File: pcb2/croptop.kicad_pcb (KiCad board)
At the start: 4 copper layers, 115.6 x 45.7 mm, 241 parts, among them J1 PICKit Header, J2 USB_A, J3 5V USB, J4 4-1734839-0, J5 Terminal Block, J6 DNP, J7 DNP, SW1 BTNA, SW2 BTNA, U1 PIC32MX795F512L, U10 AD7799, U11 74HCT125D, U12 Si7006-A20, U13 UCAM-M8Q, U14 W25N01GV, U15 LIS3DH, U16 PUSBM5V5X4, U17 DT6250-06MR-13, U18 PUSBM5V5X4, U2 REG71055, U3 FAN5333BSX, U4 MIC23050, U5 TC1014, U6 FT812Q, U8 74HCT125D, U9 DRV8872, Y1 CXO, Y2 12MHz

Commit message: Footprints done, board started
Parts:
- moved G*** 231.4 mm to (314.9, 130.8)
- moved G*** 201.3 mm to (333.2, 137.6)
- moved G*** 190.2 mm to (320.4, 156.0)
- moved G*** 169.3 mm to (314.4, 124.1)
- moved G*** 155.3 mm to (314.7, 139.0)
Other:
- board text added: "CROPTOP v2.0"

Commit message: Board almost done
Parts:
- removed C4: 26pF, Capacitor_SMD:C_0402_1005Metric
- removed D25: LED1, LED_SMD:LED_0805_2012Metric
- removed the G*** at (314.7, 139.0)
- removed the G*** at (314.4, 124.1)
- removed the G*** at (314.9, 130.8)
- removed TP100, TP73, TP74, TP78, TP82, TP83, TP85, TP86, TP88, TP89, TP90, TP91, TP92, TP99: TestPoint_Alt, croptop:TestPoint
- added C29: 0.1u, Capacitor_SMD:C_0402_1005Metric, F.Cu at (200.0, 109.0)
- added C31: 10u, Capacitor_SMD:C_1206_3216Metric, F.Cu at (201.3, 135.9)
- added C41: 0.1u, Capacitor_SMD:C_0402_1005Metric, F.Cu at (158.6, 83.1)
- added C42: 0.1u, Capacitor_SMD:C_0402_1005Metric, F.Cu at (162.1, 79.5)
- added C48: 10u, Capacitor_SMD:C_1206_3216Metric, F.Cu at (125.7, 137.8)
- added C55: 0.1u, Capacitor_SMD:C_0402_1005Metric, F.Cu at (174.0, 144.1)
- added C62: 10u, Capacitor_SMD:C_1206_3216Metric, F.Cu at (164.5, 145.4)
- added C64: 0.1u, Capacitor_SMD:C_0402_1005Metric, F.Cu at (207.0, 146.7)
- added C66: 10u, Capacitor_SMD:C_1206_3216Metric, F.Cu at (221.6, 148.6)
- added C67: 0.01u, Capacitor_SMD:C_0402_1005Metric, F.Cu at (79.4, 146.7)
- added C70: 0.1u, Capacitor_SMD:C_0805_2012Metric, F.Cu at (101.6, 137.8)
- added C72: 10u, Capacitor_SMD:C_1206_3216Metric, F.Cu at (215.9, 148.0)
- added C73: 100u, Capacitor_SMD:CP_Elec_6.3x7.7, F.Cu at (95.2, 138.4)
- added C74: 0.1u, Capacitor_SMD:C_0402_1005Metric, F.Cu at (90.8, 145.4)
- added C75: 0.1u, Capacitor_SMD:C_0402_1005Metric, F.Cu at (218.4, 151.1)
- added C76: 0.1u, Capacitor_SMD:C_0402_1005Metric, F.Cu at (90.8, 144.1)
- added C77: 0.1u, Capacitor_SMD:C_0402_1005Metric, F.Cu at (90.8, 142.9)
- added C78: 10u, Capacitor_SMD:C_1206_3216Metric, F.Cu at (77.5, 85.1)
- added C79: 10u, Capacitor_SMD:C_1206_3216Metric, F.Cu at (78.7, 79.4)
- added C80: 10u, Capacitor_SMD:C_1206_3216Metric, F.Cu at (77.5, 92.7)
- added C81: 0.1u, Capacitor_SMD:C_0402_1005Metric, F.Cu at (74.9, 87.6)
- added C82: 10u, Capacitor_SMD:C_1206_3216Metric, F.Cu at (83.8, 76.8)
- added C83: 10u, Capacitor_SMD:C_1206_3216Metric, F.Cu at (83.8, 62.9)
- added C84: 10u, Capacitor_SMD:C_1206_3216Metric, F.Cu at (78.7, 61.6)
- added C85: 10u, Capacitor_SMD:C_1206_3216Metric, F.Cu at (125.7, 64.8)
- added C86: 0.1u, Capacitor_SMD:C_0402_1005Metric, F.Cu at (125.7, 66.7)
- added C87: 0.1u, Capacitor_SMD:C_0402_1005Metric, F.Cu at (148.6, 63.5)
- added C88: 0.1u, Capacitor_SMD:C_0402_1005Metric, F.Cu at (117.9, 66.6)
- added C89: 10u, Capacitor_SMD:C_1206_3216Metric, F.Cu at (117.9, 64.8)
- added D10: TPD2E007, Package_TO_SOT_SMD:SOT-323_SC-70, F.Cu at (185.2, 89.9)
- added D11: TPD1E6B06, Diode_SMD:D_0201_0603Metric, F.Cu at (184.7, 92.7)
- added D12: TPD1E6B06, Diode_SMD:D_0201_0603Metric, F.Cu at (143.5, 148.6)
- added D13: TPD1E6B06, Diode_SMD:D_0201_0603Metric, F.Cu at (125.7, 148.6)
- added D14: TPD1E6B06, Diode_SMD:D_0201_0603Metric, F.Cu at (164.5, 148.6)
- added D15: NSR0240HT1G, Diode_SMD:D_SMA, F.Cu at (98.4, 143.8)
- added D16: TPD1E6B06, Diode_SMD:D_0201_0603Metric, F.Cu at (218.4, 152.4)
- added D17: TPD2E007, Package_TO_SOT_SMD:SOT-323_SC-70, F.Cu at (109.2, 149.2)
- added D18: TPD2E007, Package_TO_SOT_SMD:SOT-323_SC-70, F.Cu at (96.5, 149.2)
- added D19: TPD2E007, Package_TO_SOT_SMD:SOT-323_SC-70, F.Cu at (91.4, 149.2)
- added D20: TPD2E007, Package_TO_SOT_SMD:SOT-323_SC-70, F.Cu at (78.7, 149.2)
- added D21: TPD1E6B06, Diode_SMD:D_0201_0603Metric, F.Cu at (73.7, 87.3)
- added D22: LTSTC190KGKT, LED_SMD:LED_0603_1608Metric, F.Cu at (73.3, 102.5)
- added D23: LTSTC190KGKT, LED_SMD:LED_0603_1608Metric, F.Cu at (80.9, 102.5)
- added D3: TPD1E6B06, Diode_SMD:D_0201_0603Metric, F.Cu at (236.9, 94.3)
- added D4: LTSTC190KGKT, LED_SMD:LED_0603_1608Metric, F.Cu at (200.7, 123.1)
- added D5: NSR0240HT1G, Diode_SMD:D_SMA, F.Cu at (195.6, 105.4)
- added D6: TPD1E6B06, Diode_SMD:D_0201_0603Metric, F.Cu at (228.7, 126.8)
- added D8: LTSTC190KGKT, LED_SMD:LED_0603_1608Metric, F.Cu at (200.7, 126.2)
- added F1: MF-NSMF110, croptop:Bourns_Fuse, F.Cu at (233.7, 96.5)
- added J10: 1702474, croptop:solderless_terminal, F.Cu at (209.6, 158.1)
- added J11: 1702474, croptop:solderless_terminal, F.Cu at (191.8, 158.1)
- added J12: 1702474, croptop:solderless_terminal, F.Cu at (174.0, 158.1)
- added J13: 1702474, croptop:solderless_terminal, F.Cu at (102.9, 158.1)
- added J14: 1702474, croptop:solderless_terminal, F.Cu at (85.1, 158.1)
- added J15: TSM-112-01-L-DV, Connector_PinHeader_2.54mm:PinHeader_2x12_P2.54mm_Vertical_SMD, F.Cu at (97.2, 69.8)
- added J16: DM3D-SF, Connector_Card:microSD_HC_Hirose_DM3D-SF, F.Cu at (62.2, 92.1)
- added J8: 1702474, croptop:solderless_terminal, F.Cu at (138.4, 158.1)
- added J9: 1702474, croptop:solderless_terminal, F.Cu at (120.7, 158.1)
- added JP1: Solder Jumper, Jumper:SolderJumper-3_P1.3mm_Bridged12_RoundedPad1.0x1.5mm, F.Cu at (169.5, 135.9)
- added L10: BKP1005HS121, Inductor_SMD:L_0402_1005Metric, F.Cu at (150.5, 64.8)
- added L4: BKP1005HS121, Inductor_SMD:L_0402_1005Metric, F.Cu at (197.6, 133.3)
- added L5: BLM15HD102SN1D, Inductor_SMD:L_0402_1005Metric, F.Cu at (145.8, 69.3)
- added L6: BLM15HD102SN1D, Inductor_SMD:L_0402_1005Metric, F.Cu at (145.8, 66.3)
- added L7: BLM15HD102SN1D, Inductor_SMD:L_0402_1005Metric, F.Cu at (145.8, 65.3)
- added L8: BLM15HD102SN1D, Inductor_SMD:L_0402_1005Metric, F.Cu at (131.3, 68.3)
- added L9: BLM15HD102SN1D, Inductor_SMD:L_0402_1005Metric, F.Cu at (138.4, 74.7)
- added Q1: BSS138, Package_TO_SOT_SMD:SOT-23, F.Cu at (102.9, 132.1)
- added Q2: BSS84, Package_TO_SOT_SMD:SOT-23, F.Cu at (108.0, 132.1)
- added Q3: Q2319ADS-T1-GE3, Package_TO_SOT_SMD:SOT-23, F.Cu at (100.3, 148.0)
- added Q4: BSS138, Package_TO_SOT_SMD:SOT-23, F.Cu at (72.0, 106.4)
- added Q5: BSS138, Package_TO_SOT_SMD:SOT-23, F.Cu at (80.2, 106.4)
- added Q6: BSS138, Package_TO_SOT_SMD:SOT-23, F.Cu at (87.5, 106.4)
- added R100: 220, Resistor_SMD:R_0402_1005Metric, F.Cu at (111.1, 76.8)
- added R101: 220, Resistor_SMD:R_0402_1005Metric, F.Cu at (111.1, 62.9)
- added R102: 22, Resistor_SMD:R_0402_1005Metric, F.Cu at (69.8, 95.9)
- added R103: 22, Resistor_SMD:R_0402_1005Metric, F.Cu at (69.8, 90.8)
- added R104: 220, Resistor_SMD:R_0402_1005Metric, F.Cu at (108.6, 62.9)
- added R105: 22, Resistor_SMD:R_0402_1005Metric, F.Cu at (69.8, 93.3)
- added R106: 22, Resistor_SMD:R_0402_1005Metric, F.Cu at (69.8, 88.3)
- added R107: 220, Resistor_SMD:R_0402_1005Metric, F.Cu at (90.8, 63.0)
- added R108: 220, Resistor_SMD:R_0402_1005Metric, F.Cu at (95.9, 63.0)
- added R109: 220, Resistor_SMD:R_0402_1005Metric, F.Cu at (101.0, 62.9)
- added R110: 220, Resistor_SMD:R_0402_1005Metric, F.Cu at (106.0, 62.9)
- added R111: 220, Resistor_SMD:R_0402_1005Metric, F.Cu at (88.3, 63.0)
- added R112: 220, Resistor_SMD:R_0402_1005Metric, F.Cu at (93.3, 63.0)
- added R113: 220, Resistor_SMD:R_0402_1005Metric, F.Cu at (98.4, 62.9)
- added R114: 220, Resistor_SMD:R_0402_1005Metric, F.Cu at (103.5, 62.9)
- added R115: 10k, Resistor_SMD:R_0402_1005Metric, F.Cu at (78.7, 64.8)
- added R116: 100, Resistor_SMD:R_0402_1005Metric, F.Cu at (69.0, 105.1)
- added R117: 10k, Resistor_SMD:R_0402_1005Metric, F.Cu at (69.0, 108.9)
- added R118: 100, Resistor_SMD:R_0402_1005Metric, F.Cu at (70.1, 103.2)
- added R119: 100, Resistor_SMD:R_0402_1005Metric, F.Cu at (76.8, 105.1)
- added R120: 10k, Resistor_SMD:R_0402_1005Metric, F.Cu at (76.8, 108.9)
- added R121: 100, Resistor_SMD:R_0402_1005Metric, F.Cu at (78.2, 103.2)
- added R122: 100, Resistor_SMD:R_0402_1005Metric, F.Cu at (84.3, 105.1)
- added R123: 10k, Resistor_SMD:R_0402_1005Metric, F.Cu at (84.5, 108.9)
- added R124: 100, Resistor_SMD:R_0402_1005Metric, F.Cu at (85.9, 103.2)
- added R125: 10k, Resistor_SMD:R_0402_1005Metric, F.Cu at (89.9, 118.4)
- added R126: 10k, Resistor_SMD:R_0402_1005Metric, F.Cu at (89.9, 113.5)
- added R127: 10k, Resistor_SMD:R_0402_1005Metric, F.Cu at (89.9, 108.8)
- added R128: 10k, Resistor_SMD:R_0402_1005Metric, F.Cu at (89.9, 111.1)
- added R129: 10k, Resistor_SMD:R_0402_1005Metric, F.Cu at (89.9, 116.0)
- added R130: 10k, Resistor_SMD:R_0402_1005Metric, F.Cu at (89.9, 120.8)
- added R2: 100, Resistor_SMD:R_0402_1005Metric, F.Cu at (101.0, 128.3)
- added R3: 100, Resistor_SMD:R_0402_1005Metric, F.Cu at (109.9, 128.3)
- added R4: 10k, Resistor_SMD:R_0402_1005Metric, F.Cu at (150.5, 115.8)
- added R48: 22, Resistor_SMD:R_0402_1005Metric, F.Cu at (185.4, 68.1)
- added R49: 22, Resistor_SMD:R_0402_1005Metric, F.Cu at (191.8, 68.1)
- added R58: 22, Resistor_SMD:R_0402_1005Metric, F.Cu at (187.3, 134.6)
- added R59: 22, Resistor_SMD:R_0402_1005Metric, F.Cu at (187.3, 136.5)
- added R60: 22, Resistor_SMD:R_0402_1005Metric, F.Cu at (187.3, 138.4)
- added R61: 10k, Resistor_SMD:R_0402_1005Metric, F.Cu at (141.0, 142.2)
- added R64: 220, Resistor_SMD:R_0402_1005Metric, F.Cu at (157.5, 149.2)
- added R65: 220, Resistor_SMD:R_0402_1005Metric, F.Cu at (154.9, 149.2)
- added R68: 220, Resistor_SMD:R_0402_1005Metric, F.Cu at (121.9, 149.2)
- added R69: 220, Resistor_SMD:R_0402_1005Metric, F.Cu at (119.4, 149.2)
- added R78: 10k, Resistor_SMD:R_0402_1005Metric, F.Cu at (116.8, 135.3)
- added R79: 22, Resistor_SMD:R_0402_1005Metric, F.Cu at (117.5, 138.4)
- added R80: 22, Resistor_SMD:R_0402_1005Metric, F.Cu at (117.5, 139.7)
- added R81: 10k, Resistor_SMD:R_0402_1005Metric, F.Cu at (219.7, 144.8)
- added R82: 0.2, Resistor_SMD:R_2512_6332Metric, F.Cu at (114.9, 148.6)
- added R83: 0.2, Resistor_SMD:R_2512_6332Metric, F.Cu at (114.9, 144.1)
- added R84: 1M, Resistor_SMD:R_0402_1005Metric, F.Cu at (77.3, 141.0)
- added R85: 10k, Resistor_SMD:R_0402_1005Metric, F.Cu at (99.7, 141.0)
- added R86: 0.2, Resistor_SMD:R_2512_6332Metric, F.Cu at (73.0, 154.4)
- added R87: 0.2, Resistor_SMD:R_2512_6332Metric, F.Cu at (74.7, 143.5)
- added R88: 10k, Resistor_SMD:R_0402_1005Metric, F.Cu at (86.4, 80.0)
- added R89: 220, Resistor_SMD:R_0402_1005Metric, F.Cu at (88.3, 76.8)
- added R90: 220, Resistor_SMD:R_0402_1005Metric, F.Cu at (93.3, 76.8)
- added R91: 220, Resistor_SMD:R_0402_1005Metric, F.Cu at (98.4, 76.8)
- added R92: 220, Resistor_SMD:R_0402_1005Metric, F.Cu at (103.5, 76.8)
- added R93: 220, Resistor_SMD:R_0402_1005Metric, F.Cu at (90.8, 76.8)
- added R94: 220, Resistor_SMD:R_0402_1005Metric, F.Cu at (95.9, 76.8)
- added R95: 220, Resistor_SMD:R_0402_1005Metric, F.Cu at (101.0, 76.8)
- added R96: 220, Resistor_SMD:R_0402_1005Metric, F.Cu at (106.0, 76.8)
- added R97: 220, Resistor_SMD:R_0402_1005Metric, F.Cu at (78.1, 95.9)
- added R98: 220, Resistor_SMD:R_0402_1005Metric, F.Cu at (108.6, 76.8)
- added R99: 10k, Resistor_SMD:R_0402_1005Metric, F.Cu at (75.6, 96.5)
- added SW3: SW_Push, Button_Switch_SMD:SW_SPST_PTS645, F.Cu at (76.8, 114.3)
- added SW4: SW_Push, Button_Switch_SMD:SW_SPST_PTS645, F.Cu at (84.5, 114.3)
- added TP4: TestPoint, croptop:TestPoint, F.Cu at (126.1, -6.08)
- added TP47: TestPoint, croptop:TestPoint, F.Cu at (170.7, -13.7)
- added TP48: TestPoint, croptop:TestPoint, F.Cu at (142.6, -10.1)
- added TP49: TestPoint, croptop:TestPoint, F.Cu at (138.5, -10.1)
- added TP50: TestPoint, croptop:TestPoint, F.Cu at (99.2, -3.93)
- added TP51: TestPoint, croptop:TestPoint, F.Cu at (101.8, -5.98)
- added TP52: TestPoint, croptop:TestPoint, F.Cu at (113.7, -18.1)
- added TP53: TestPoint, croptop:TestPoint, F.Cu at (120.8, -14.4)
- added TP54: TestPoint, croptop:TestPoint, F.Cu at (122.8, -16.5)
- added TP55: TestPoint, croptop:TestPoint, F.Cu at (108.6, -13.6)
- added TP56: TestPoint, croptop:TestPoint, F.Cu at (115.8, -20.4)
- added TP57: TestPoint, croptop:TestPoint, F.Cu at (175.3, -11.2)
- added TP58: TestPoint, croptop:TestPoint, F.Cu at (117.9, -23.0)
- added TP59: TestPoint, croptop:TestPoint, F.Cu at (111.6, -16.0)
- added TP63: TestPoint, croptop:TestPoint, F.Cu at (115.8, -22.4)
- added TP67: TestPoint, croptop:TestPoint, F.Cu at (122.8, -14.4)
- added TP69: TestPoint, croptop:TestPoint, F.Cu at (112.6, -6.34)
- added U19: AP22802AW5, Package_TO_SOT_SMD:SOT-23-5, F.Cu at (143.7, 142.2)
- added U20: AD7799, Package_SO:TSSOP-16_4.4x5mm_P0.65mm, F.Cu at (191.8, 137.2)
- added U21: AP22802AW5, Package_TO_SOT_SMD:SOT-23-5, F.Cu at (125.7, 142.2)
- added U22: TPD4E1U06DBV, Package_TO_SOT_SMD:SOT-23-6, F.Cu at (147.3, 148.6)
- added U23: AP22802AW5, Package_TO_SOT_SMD:SOT-23-5, F.Cu at (164.5, 142.2)
- added U24: TPD4E1U06DBV, Package_TO_SOT_SMD:SOT-23-6, F.Cu at (129.5, 148.6)
- added U25: TPD4E1U06DBV, Package_TO_SOT_SMD:SOT-23-6, F.Cu at (182.9, 148.3)
- added U26: TPD4E1U06DBV, Package_TO_SOT_SMD:SOT-23-6, F.Cu at (200.7, 148.3)
- added U27: DRV8872, croptop:8-PowerSOIC, F.Cu at (112.4, 139.1)
- added U28: DRV8825, Package_SO:HTSSOP-28-1EP_4.4x9.7mm_P0.65mm_EP3.4x9.5mm_Mask2.4x6.17mm_ThermalVias, F.Cu at (84.5, 142.2)
- added U29: AP22802AW5, Package_TO_SOT_SMD:SOT-23-5, F.Cu at (219.1, 148.6)
- added U30: TPD4E1U06DBV, Package_TO_SOT_SMD:SOT-23-6, F.Cu at (92.1, 80.6)
- added U31: TPD4E1U06DBV, Package_TO_SOT_SMD:SOT-23-6, F.Cu at (102.2, 80.6)
- added U32: AP22802AW5, Package_TO_SOT_SMD:SOT-23-5, F.Cu at (77.5, 88.3)
- added U33: AP22802AW5, Package_TO_SOT_SMD:SOT-23-5, F.Cu at (83.8, 80.0)
- added U34: TPD4E1U06DBV, Package_TO_SOT_SMD:SOT-23-6, F.Cu at (109.9, 80.6)
- added U35: TPD4E1U06DBV, Package_TO_SOT_SMD:SOT-23-6, F.Cu at (61.0, 101.0)
- added U36: AP22802AW5, Package_TO_SOT_SMD:SOT-23-5, F.Cu at (83.8, 59.7)
- added U37: TPD4E1U06DBV, Package_TO_SOT_SMD:SOT-23-6, F.Cu at (92.1, 59.1)
- added U38: TPD4E1U06DBV, Package_TO_SOT_SMD:SOT-23-6, F.Cu at (102.2, 59.1)
- added U39: LIS3DSHTR, croptop:LISDR, F.Cu at (126.4, 69.2)
- added U40: CAM-M8C-0, croptop:GPS, F.Cu at (138.4, 65.4)
- added U41: Si7006-A20, croptop:SI7006, F.Cu at (117.9, 69.2)
- added U7: TPD4E1U06DBV, Package_TO_SOT_SMD:SOT-23-6, F.Cu at (224.4, 116.5)
- C1, C10, C12, C19, C20, C21, C25, C28, C46, C52, C56, C58, C61: value 0.1uF -> 10u; footprint Capacitor_SMD:C_0402_1005Metric -> Capacitor_SMD:C_1206_3216Metric
- C11, C13, C40: value 0.1uF -> 27p
- C14, C22, C23: value 1uF -> 0.1u
- C15, C2, C5: value 10uF -> 0.1u; footprint Capacitor_SMD:C_0805_2012Metric -> Capacitor_SMD:C_0402_1005Metric
- C16, C17: value 10uF -> 100u; footprint Capacitor_SMD:C_0805_2012Metric -> Capacitor_SMD:CP_Elec_6.3x7.7
- C18: value 100uF -> 10u; footprint Capacitor_SMD:CP_Elec_6.3x7.7 -> Capacitor_SMD:C_1206_3216Metric
- C24: value 560pF -> 10u; footprint Capacitor_SMD:C_0603_1608Metric -> Capacitor_SMD:C_1206_3216Metric
- C26: value 470pF -> 10u; footprint Capacitor_SMD:C_0402_1005Metric -> Capacitor_SMD:C_1206_3216Metric
- C27: value 0.1uF -> 0.1u; footprint Capacitor_SMD:C_0805_2012Metric -> Capacitor_SMD:C_0402_1005Metric
- C3, C33, C35, C36, C44, C49, C53, C54, C57, C59, C60, C63, C65, C69, C7, C8, C9: value 0.1uF -> 0.1u
- C30: value 1uF -> 10u; footprint Capacitor_SMD:C_0402_1005Metric -> Capacitor_SMD:C_1206_3216Metric
- C32, C43, C45, C51: value 10uF -> 10u; footprint Capacitor_SMD:C_0805_2012Metric -> Capacitor_SMD:C_1206_3216Metric
- C34: value 0.1uF -> 100u; footprint Capacitor_SMD:C_0402_1005Metric -> Capacitor_SMD:CP_Elec_6.3x7.7
- C37, C39, C6: value 26pF -> 0.1u
- C38: value 10uF -> 27p; footprint Capacitor_SMD:C_0805_2012Metric -> Capacitor_SMD:C_0402_1005Metric
- C47: value 0.1uF -> 10u; footprint Capacitor_SMD:C_0805_2012Metric -> Capacitor_SMD:C_1206_3216Metric
- C50: value 100uF -> 0.1u; footprint Capacitor_SMD:CP_Elec_6.3x7.7 -> Capacitor_SMD:C_0402_1005Metric
- C68, C71: value 0.1uF -> 0.1u; footprint Capacitor_SMD:C_0402_1005Metric -> Capacitor_SMD:C_0805_2012Metric
- D1: value BAT42W -> LTSTC190KGKT; footprint croptop:D_SOD-123 -> LED_SMD:LED_0603_1608Metric
- D2: value 3SMAJ5935B -> LTSTC190KRKT; footprint croptop:DO-214AC -> LED_SMD:LED_0603_1608Metric
- D24: value LED2 -> LTSTC190KGKT; footprint LED_SMD:LED_0805_2012Metric -> LED_SMD:LED_0603_1608Metric
- D7: value LED1 -> LTSTC190KGKT; footprint LED_SMD:LED_0805_2012Metric -> LED_SMD:LED_0603_1608Metric
- D9: value SBRD10200TR -> LTSTC190KGKT; footprint croptop:SizeOfThisLad -> LED_SMD:LED_0603_1608Metric
- FID1, FID2: value FIDUCIAL -> Fiducial
- G***: moved to F.Cu
- H1: value Top Left -> 3mm; footprint MountingHole:MountingHole_4mm_Pad -> MountingHole:MountingHole_3mm_Pad_Via
- H2: value Bottom Left -> 3mm; footprint MountingHole:MountingHole_4mm_Pad -> MountingHole:MountingHole_3mm_Pad_Via
- H3: value Top Right -> 3mm; footprint MountingHole:MountingHole_4mm_Pad -> MountingHole:MountingHole_3mm_Pad_Via
- H4: value Bottom Right -> 3mm; footprint MountingHole:MountingHole_4mm_Pad -> MountingHole:MountingHole_3mm_Pad_Via
- J1: value PICKit Header -> TSM-106-01-L-SV; footprint Connector_PinHeader_2.54mm:PinHeader_1x06_P2.54mm_Vertical -> Connector_PinHeader_2.54mm:PinHeader_1x06_P2.54mm_Vertical_SMD_Pin1Right
- J2: value USB_A -> 0473460001; footprint croptop:USB_A_Assmann_Horizontal -> Connector_USB:USB_Micro-B_Molex_47346-0001
- J3: value 5V USB -> 87583-2010BLF; footprint croptop:USB_Micro-B_Molex_47346-0001 -> croptop:87583-2010BLF
- J4: value 4-1734839-0 -> TSM-102-01-L-DV; footprint croptop:4-1734839-0 -> Connector_PinHeader_2.54mm:PinHeader_2x02_P2.54mm_Vertical_SMD
- J5: value Terminal Block -> 686104183422; footprint TerminalBlock_4Ucon:TerminalBlock_4Ucon_1x15_P3.50mm_Horizontal -> croptop:TE_84952-4_1x04-1MP_P1.0mm_Horizontal
- J6: value DNP -> 62684-402100ALF; footprint Connector_PinHeader_2.54mm:PinHeader_1x04_P2.54mm_Vertical -> Connector_FFC-FPC:Hirose_FH12-40S-0.5SH_1x40-1MP_P0.50mm_Horizontal
- J7: value DNP -> 1702474; footprint Connector_PinHeader_2.54mm:PinHeader_1x04_P2.54mm_Vertical -> croptop:solderless_terminal
- L1: value 10uH -> BKP1005HS121; footprint Inductor_SMD:L_1210_3225Metric -> Inductor_SMD:L_0402_1005Metric
- L2: value 10uH -> 4.7u; footprint Inductor_SMD:L_1210_3225Metric -> Inductor_SMD:L_Bourns_SRN6045TA
- L3: value 1uH -> 2.2u; footprint Inductor_SMD:L_0805_2012Metric -> Inductor_SMD:L_Bourns_SRN6045TA
- R10, R12, R13, R20, R21, R5, R6, R7, R76, R77, R8, R9: value 33 -> 10k
- R11, R15, R16, R17, R18: value 33 -> 220
- R14: value 33 -> 1.1
- R19, R73, R74, R75: value 33 -> 100
- R22, R23, R29, R30, R31, R32, R33: value 33 -> 22
- R24, R25: value 2K -> 22
- R26, R34, R35, R36, R37, R54, R55: value 10 -> 22
- R27, R50, R51: value 0 -> 22
- R28: value 2.2 -> 22
- R38, R39, R40, R41, R42, R43, R44, R45, R46, R47: value 100 -> 22
- R52, R53: value 220 -> 22
- R56, R57: value 10k -> 22
- R66, R67: value 60 -> 220
- R70: value 0 -> 100
- R71: value 60 -> 100
- SW1, SW2: value BTNA -> SW_Push
- TP1, TP10, TP11, TP12, TP13, TP14, TP15, TP16, TP17, TP18, TP19, TP2, TP20, TP21, TP22, TP23, TP24, TP25, TP26, TP27, TP28, TP29, TP3, TP30, TP31, TP32, TP33, TP34, TP35, TP36, TP37, TP38, TP39, TP40, TP41, TP42, TP43, TP44, TP45, TP46, TP5, TP6, TP60, TP61, TP62, TP64, TP65, TP66, TP68, TP7, TP70, TP71, TP72, TP8, TP9: value TestPoint_Alt -> TestPoint; moved to F.Cu
- U10: value AD7799 -> TPD4E1U06DBV; footprint Package_SO:TSSOP-16_4.4x5mm_P0.65mm -> Package_TO_SOT_SMD:SOT-23-6
- U11, U8: value 74HCT125D -> TPD4E1U06DBV; footprint Package_SO:SOIC-14_3.9x8.7mm_P1.27mm -> Package_TO_SOT_SMD:SOT-23-6
- U12: value Si7006-A20 -> TPD4E1U06DBV; footprint croptop:SI7006 -> Package_TO_SOT_SMD:SOT-23-6
- U13: value UCAM-M8Q -> TPD4E1U06DBV; footprint croptop:GPS -> Package_TO_SOT_SMD:SOT-23-6
- U14: value W25N01GV -> TPD4E1U06DBV; footprint croptop:W25N01GV -> Package_TO_SOT_SMD:SOT-23-6
- U15: value LIS3DH -> TPD4E1U06DBV; footprint Package_LGA:LGA-16_3x3mm_P0.5mm_LayoutBorder3x5y -> Package_TO_SOT_SMD:SOT-23-6
- U16: value PUSBM5V5X4 -> TPD4E1U06DBV; footprint croptop:PUSBM5V5X4 -> Package_TO_SOT_SMD:SOT-23-6
- U17: value DT6250-06MR-13 -> TPD4E1U06DBV; footprint Package_SO:MSOP-8_3x3mm_P0.65mm -> Package_TO_SOT_SMD:SOT-23-6
- U18: value PUSBM5V5X4 -> 74HCT125D653; footprint croptop:PUSBM5V5X4 -> Package_SO:SOIC-14_3.9x8.7mm_P1.27mm
- U2: value REG71055 -> REG71055DDC
- U3: value FAN5333BSX -> AP22802AW5
- U4: value MIC23050 -> TPS61169DCK; footprint Package_DFN_QFN:DFN-8-1EP_2x2mm_P0.45mm_EP0.64x1.38mm -> Package_TO_SOT_SMD:SOT-353_SC-70-5
- U5: value TC1014 -> TPS62131RGT; footprint Package_TO_SOT_SMD:SOT-23-5 -> Package_DFN_QFN:QFN-16-1EP_3x3mm_P0.5mm_EP1.8x1.8mm
- U6: value FT812Q -> TPS70950DBV; footprint Package_DFN_QFN:QFN-56-1EP_8x8mm_P0.5mm_EP4.5x5.2mm -> Package_TO_SOT_SMD:SOT-23-5
- U9: value DRV8872 -> FT812Q; footprint croptop:8-PowerSOIC -> Package_DFN_QFN:QFN-56-1EP_8x8mm_P0.5mm_EP4.5x5.2mm
- Y1: value CXO -> ABLS-8.000MHZ-B4-T
- Y2: value 12MHz -> ABLS-12.000MHZ-B2-T
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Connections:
- net PKT_PGEC renamed PICKIT_PGEC
- net PKT_PGED renamed PICKIT_PGED
- C1 pad 1: Net-(C1-Pad1) -> +3V3
- C1 pad 2: DRV_GND -> DGND
- C10 pad 1: DVDD -> Net-(C10-Pad1)
- C10 pad 2: DRV_GND -> DGND
- C11 pad 1: DVDD -> Net-(C11-Pad1)
- C11 pad 2: DRV_GND -> DGND
- C12 pad 1: DVDD -> Net-(C12-Pad1)
- C12 pad 2: DRV_GND -> DGND
- C13 pad 1: DVDD -> Net-(C13-Pad1)
- C13 pad 2: DRV_GND -> DGND
- C14 pad 1: DVDD_UNREG -> Net-(C14-Pad1)
- C14 pad 2: DRV_GND -> DGND
- C15 pad 1: DVDD_UNREG -> PICKIT_MCLR
- C15 pad 2: DRV_GND -> DGND
- C16 pad 1: DVDD_UNREG -> +5V
- C16 pad 2: DRV_GND -> DGND
- C17 pad 1: DVDD_UNREG -> +5V
- C17 pad 2: DRV_GND -> DGND
- C18 pad 1: DVDD_UNREG -> +5V
- C18 pad 2: DRV_GND -> DGND
- C19 pad 1: Net-(C19-Pad1) -> +5V
- C19 pad 2: Net-(C19-Pad2) -> DGND
- C2 pad 1: Net-(C2-Pad1) -> +3V3
- C2 pad 2: DRV_GND -> DGND
- C20 pad 1: DVDD_UNREG -> +5V
- C20 pad 2: DRV_GND -> DGND
- C21 pad 1: DVDD_UNREG -> +5V
- C21 pad 2: DRV_GND -> DGND
- C22 pad 2: DRV_GND -> Net-(C22-Pad2)
- C23 pad 1: Net-(C22-Pad1) -> Net-(C23-Pad1)
- C23 pad 2: DRV_GND -> DGND
- C24 pad 2: DVDD -> DGND
- C25 pad 1: DVDD -> USB_PWR_SENSE
- C25 pad 2: DRV_GND -> DGND
- C26 pad 1: Net-(C26-Pad1) -> Net-(C24-Pad1)
- C26 pad 2: DRV_GND -> DGND
- C27 pad 1: LCD_ANODE -> USB_PWR_SENSE
- C27 pad 2: DRV_GND -> DGND
- C28 pad 1: LCD_CATHODE -> LCD_A
- C28 pad 2: DRV_GND -> DGND
- C3 pad 1: DVDD -> +3V3
- C3 pad 2: DRV_GND -> DGND
- C30 pad 1: ADC_VDD -> +3V3
- C30 pad 2: DRV_GND -> DGND
- C32 pad 1: DVDD -> +3V3
- C32 pad 2: DRV_GND -> DGND
- C33 pad 1: DVDD -> +5V_REG
- C33 pad 2: DRV_GND -> DGND
- C34 pad 1: DVDD -> +3V3
- C34 pad 2: DRV_GND -> DGND
- C35 pad 1: DVDD -> DGND
- C35 pad 2: DRV_GND -> Net-(C35-Pad2)
- C36 pad 1: DVDD -> ~GPU_PWR_DWN
- C36 pad 2: DRV_GND -> DGND
- C37 pad 1: Net-(C37-Pad1) -> +3V3
- C37 pad 2: DRV_GND -> DGND
- C38 pad 2: DRV_GND -> DGND
- C39 pad 1: Net-(C39-Pad1) -> +3V3
- C39 pad 2: DRV_GND -> DGND
- C40 pad 1: Net-(C38-Pad1) -> Net-(C40-Pad1)
- C40 pad 2: DRV_GND -> DGND
- C43 pad 1: DVDD -> Net-(C43-Pad1)
- C43 pad 2: DRV_GND -> DGND
- C44 pad 1: DVDD -> Net-(C43-Pad1)
- C44 pad 2: DRV_GND -> DGND
- C45 pad 1: DVDD -> +3V3
- C45 pad 2: DRV_GND -> DGND
- C46 pad 1: DVDD -> +3V3
- C46 pad 2: DRV_GND -> DGND
- C47 pad 1: Net-(C47-Pad1) -> +3V3
- C47 pad 2: DRV_GND -> DGND
- C49 pad 1: ADC_VDD -> +3V3
- C49 pad 2: DRV_GND -> DGND
- C5 pad 1: DVDD -> +3V3
- C5 pad 2: DRV_GND -> DGND
- C50 pad 1: Net-(C47-Pad1) -> Net-(C50-Pad1)
- C50 pad 2: DRV_GND -> DGND
- C51 pad 1: ADC_VDD -> Net-(C51-Pad1)
- C51 pad 2: DRV_GND -> DGND
- C52 pad 2: Net-(C52-Pad2) -> DGND
- C56 pad 1: DRV_GND -> Net-(C56-Pad1)
- C56 pad 2: Net-(C54-Pad2) -> DGND
- C57 pad 1: DRV_GND -> DGND
- C57 pad 2: Net-(C54-Pad1) -> Net-(C55-Pad1)
- C58 pad 1: DRV_GND -> POTEN_ADC_2
- C58 pad 2: Net-(C53-Pad2) -> DGND
- C59 pad 1: DRV_GND -> DGND
- C59 pad 2: Net-(C53-Pad1) -> Net-(C55-Pad2)
- C6 pad 1: Net-(C6-Pad1) -> +3V3
- C6 pad 2: DRV_GND -> DGND
- C60 pad 1: DRV_GND -> DGND
- C60 pad 2: Net-(C52-Pad2) -> Net-(C54-Pad1)
- C61 pad 1: DRV_GND -> POTEN_ADC_1
- C61 pad 2: Net-(C52-Pad1) -> DGND
- C63 pad 1: DVDD -> DGND
- C63 pad 2: DRV_GND -> Net-(C54-Pad2)
- C65 pad 1: DVDD -> DGND
- C65 pad 2: DRV_GND -> Net-(C53-Pad2)
- C68 pad 1: DVDD -> Net-(C68-Pad1)
- C68 pad 2: DRV_GND -> DGND
- C69 pad 1: DVDD -> Net-(C69-Pad1)
- C69 pad 2: DRV_GND -> Net-(C68-Pad1)
- C7 pad 1: DVDD -> +3V3
- C7 pad 2: DRV_GND -> DGND
- C71 pad 1: DVDD -> Net-(C68-Pad1)
- C71 pad 2: DRV_GND -> DGND
- C8 pad 1: DVDD -> +3V3
- C8 pad 2: DRV_GND -> DGND
- C9 pad 1: DVDD -> Net-(C10-Pad1)
- C9 pad 2: DRV_GND -> DGND
- D1 pad 1: LCD_ANODE -> Net-(D1-Pad1)
- D2 pad 1: LCD_ANODE -> Net-(D2-Pad1)
- D2 pad 2: LCD_CATHODE -> Net-(D2-Pad2)
- D24 pad 2: LED_B -> Net-(D24-Pad2)
- D7 pad 2: DVDD_UNREG -> LCD_A
- D9 pad 1: Net-(C47-Pad1) -> Net-(D9-Pad1)
- D9 pad 2: DRV_BAT -> +3V3
- J1 pad 1: PKT_MCLR -> PICKIT_MCLR
- J1 pad 2: DVDD -> +3V3
- J1 pad 3: DRV_GND -> DGND
- J2 pad 1: DVDD_UNREG -> Net-(D3-Pad1)
- J2 pad 2: USB_D- -> Net-(J2-Pad2)
- J2 pad 3: USB_D+ -> Net-(J2-Pad3)
- J2 pad 4: DRV_GND -> Net-(J2-Pad4)
- J2 pad 5: DRV_GND -> DGND
- J3 pad 1: DVDD_UNREG -> USB_PWR_SENSE
- J3 pad 2: Net-(J3-Pad2) -> USB_D-
- J3 pad 3: Net-(J3-Pad3) -> USB_D+
- J3 pad 4: Net-(J3-Pad4) -> DGND
- J3 pad 5: DRV_GND -> Net-(C35-Pad2)
- J4 pad 1: LCD_CATHODE -> +3V3
- J4 pad 2: LCD_ANODE -> Net-(J4-Pad2)
- J4 pad 3: DRV_GND -> DGND
- J4 pad 4: DVDD -> DGND
- J5 pad 1: ADC_VDD -> GPU_X+
- J5 pad 2: ADC_GND -> GPU_Y-
- J5 pad 3: ADC_A1+ -> GPU_X-
- J5 pad 4: ADC_A1- -> GPU_Y+
- J6 pad 1: ADC_VDD -> LCD_K
- J6 pad 2: ADC_GND -> LCD_A
- J6 pad 3: Net-(J6-Pad3) -> DGND
- J6 pad 4: Net-(J6-Pad4) -> +3V3
- J7 pad 1: ADC_VDD -> Net-(C62-Pad1)
- J7 pad 2: ADC_GND -> Net-(J7-Pad2)
- J7 pad 4: Net-(J7-Pad4) -> DGND
- L1 pad 1: DVDD -> +3V3
- L1 pad 2: Net-(L1-Pad2) -> Net-(C10-Pad1)
- L2 pad 1: Net-(D1-Pad2) -> Net-(D5-Pad2)
- L2 pad 2: DVDD_UNREG -> +5V
- L3 pad 1: DVDD -> +3V3
- R1 pad 1: DVDD -> +3V3
- R1 pad 2: PKT_MCLR -> ~PWR_FAULT
- R10 pad 1: Net-(J4-Pad10) -> CONFIG_ADC
- R10 pad 2: LCD_R5 -> DGND
- R11 pad 1: Net-(J4-Pad11) -> Net-(D4-Pad1)
- R11 pad 2: LCD_R6 -> DGND
- R12 pad 1: Net-(J4-Pad12) -> USB_PWR_EN
- R12 pad 2: LCD_R7 -> DGND
- R13 pad 1: Net-(J4-Pad13) -> GPU_PWM
- R13 pad 2: LCD_G0 -> DGND
- R14 pad 1: Net-(J4-Pad14) -> LCD_K
- R14 pad 2: LCD_G1 -> DGND
- R15 pad 1: Net-(J4-Pad15) -> Net-(D7-Pad1)
- R15 pad 2: LCD_G2 -> Net-(R15-Pad2)
- R16 pad 1: Net-(J4-Pad16) -> Net-(R15-Pad2)
- R16 pad 2: LCD_G3 -> Net-(R16-Pad2)
- R17 pad 1: Net-(J4-Pad17) -> Net-(R16-Pad2)
- R17 pad 2: LCD_G4 -> DGND
- R18 pad 1: Net-(J4-Pad18) -> Net-(D8-Pad1)
- R18 pad 2: LCD_G5 -> DGND
- R19 pad 1: Net-(J4-Pad19) -> Net-(D9-Pad1)
- R19 pad 2: LCD_G6 -> DGND
- R20 pad 1: Net-(J4-Pad20) -> +3V3
- R20 pad 2: LCD_G7 -> ~GPU_PWR_DWN
- R21 pad 1: Net-(J4-Pad21) -> +3V3
- R21 pad 2: LCD_B0 -> ~GPU_INT
- R22 pad 1: Net-(J4-Pad22) -> Net-(R22-Pad1)
- R22 pad 2: LCD_B1 -> ~GPU_CS
- R23 pad 1: Net-(J4-Pad23) -> Net-(R23-Pad1)
- R23 pad 2: LCD_B2 -> GPU_MOSI
- R24 pad 1: DVDD -> Net-(R24-Pad1)
- R24 pad 2: SCL -> GPU_MISO
- R25 pad 1: DVDD -> Net-(R25-Pad1)
- R25 pad 2: SDA -> GPU_SCLK
- R26 pad 1: MISO -> Net-(J6-Pad5)
- R27 pad 1: Net-(C6-Pad1) -> Net-(J6-Pad7)
- R28 pad 1: LCD_CATHODE -> Net-(J6-Pad9)
- R28 pad 2: DRV_GND -> Net-(R28-Pad2)
- R29 pad 1: Net-(J4-Pad24) -> Net-(J6-Pad11)
- R29 pad 2: LCD_B3 -> Net-(R29-Pad2)
- R30 pad 1: Net-(J4-Pad25) -> Net-(J6-Pad13)
- R30 pad 2: LCD_B4 -> Net-(R30-Pad2)
- R31 pad 1: Net-(J4-Pad26) -> Net-(J6-Pad15)
- R31 pad 2: LCD_B5 -> Net-(R31-Pad2)
- R32 pad 1: Net-(J4-Pad27) -> Net-(J6-Pad17)
- R32 pad 2: LCD_B6 -> Net-(R32-Pad2)
- R33 pad 1: Net-(J4-Pad28) -> Net-(J6-Pad19)
- R33 pad 2: LCD_B7 -> Net-(R33-Pad2)
- R34 pad 1: Net-(R34-Pad1) -> Net-(J6-Pad21)
- R34 pad 2: SCLK -> Net-(R34-Pad2)
- R35 pad 1: Net-(R35-Pad1) -> Net-(J6-Pad23)
- R35 pad 2: MOSI -> Net-(R35-Pad2)
- R36 pad 1: Net-(R36-Pad1) -> Net-(J6-Pad25)
- R36 pad 2: DRV_IN1 -> Net-(R36-Pad2)
- R37 pad 1: Net-(R37-Pad1) -> Net-(J6-Pad27)
- R37 pad 2: DRV_IN2 -> Net-(R37-Pad2)
- R38 pad 1: Net-(R38-Pad1) -> Net-(J6-Pad30)
- R39 pad 1: Net-(R39-Pad1) -> Net-(J6-Pad32)
- R40 pad 1: Net-(R40-Pad1) -> Net-(J6-Pad34)
- R41 pad 1: Net-(R41-Pad1) -> Net-(J6-Pad6)
- R42 pad 1: ADC_A1+ -> Net-(J6-Pad8)
- R42 pad 2: Net-(C52-Pad1) -> Net-(R42-Pad2)
- R43 pad 1: Net-(J6-Pad3) -> Net-(J6-Pad10)
- R43 pad 2: Net-(C53-Pad1) -> Net-(R43-Pad2)
- R44 pad 1: Net-(J7-Pad3) -> Net-(J6-Pad12)
- R44 pad 2: Net-(C54-Pad1) -> Net-(R44-Pad2)
- R45 pad 1: ADC_A1- -> Net-(J6-Pad14)
- R45 pad 2: Net-(C52-Pad2) -> Net-(R45-Pad2)
- R46 pad 1: Net-(J6-Pad4) -> Net-(J6-Pad16)
- R46 pad 2: Net-(C53-Pad2) -> Net-(R46-Pad2)
- R47 pad 1: Net-(J7-Pad4) -> Net-(J6-Pad18)
- R47 pad 2: Net-(C54-Pad2) -> Net-(R47-Pad2)
- R5 pad 1: Net-(J4-Pad5) -> +3V3
- R5 pad 2: LCD_R0 -> PMOD_SDA
- R50 pad 1: DVDD -> Net-(J6-Pad24)
- R50 pad 2: ROT_VDD -> Net-(R50-Pad2)
- R51 pad 1: ROT_VDD -> Net-(J6-Pad26)
- R51 pad 2: DVDD_UNREG -> Net-(R51-Pad2)
- R52 pad 1: Net-(R52-Pad1) -> Net-(J6-Pad28)
- R52 pad 2: TX -> Net-(R52-Pad2)
- R53 pad 1: Net-(R53-Pad1) -> Net-(J6-Pad31)
- R53 pad 2: RX -> Net-(R53-Pad2)
- R54 pad 1: Net-(R54-Pad1) -> Net-(J6-Pad33)
- R54 pad 2: SCLK -> Net-(R54-Pad2)
- R55 pad 2: MOSI -> ENCDR_B
- R56 pad 1: BTN_A -> Net-(R56-Pad1)
- R56 pad 2: Net-(R56-Pad2) -> ENCDR_A
- R57 pad 1: BTN_B -> Net-(R57-Pad1)
- R57 pad 2: Net-(R57-Pad2) -> ADI_SCLK
- R6 pad 1: Net-(J4-Pad6) -> +3V3
- R6 pad 2: LCD_R1 -> ONBRD_SCL
- R62 pad 1: Net-(R57-Pad2) -> +3V3
- R62 pad 2: DRV_GND -> DGND
- R63 pad 1: Net-(R56-Pad2) -> Net-(C51-Pad1)
- R63 pad 2: DRV_GND -> DGND
- R66 pad 1: DRV_GND -> Net-(J8-Pad2)
- R66 pad 2: Net-(D24-Pad1) -> POTEN_ADC_1
- R67 pad 1: DRV_GND -> Net-(J8-Pad3)
- R67 pad 2: Net-(D25-Pad1) -> POTEN_ADC_2
- R7 pad 1: Net-(J4-Pad7) -> +3V3
- R7 pad 2: LCD_R2 -> ONBRD_SDA
- R70 pad 1: Net-(C1-Pad1) -> ADI_A1+
- R70 pad 2: PKT_MCLR -> Net-(C53-Pad2)
- R71 pad 1: Net-(D7-Pad1) -> ADI_A2+
- R71 pad 2: Net-(R71-Pad2) -> Net-(C54-Pad2)
- R72 pad 1: Net-(R71-Pad2) -> ADI_A3+
- R72 pad 2: DRV_GND -> Net-(C55-Pad2)
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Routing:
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- added copper zone on Vdd.Cu, net +3V3
- added copper zone on Vdd.Cu, net +5V
- added copper zone on Vdd.Cu, net +5V_REG
- added copper zone on F.Cu, net DGND
- added copper zone on Gnd.Cu, net DGND
- removed copper zone on Vdd.Cu, net ADC_VDD
- removed copper zone on Gnd.Cu, net DRV_GND
- removed copper zone on Vdd.Cu, net DVDD
- removed copper zone on Vdd.Cu, net DVDD_UNREG
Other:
- board size 115.6 x 45.7 mm -> 190.1 x 107.2 mm
- board text added: "+3V3"
- board text added: "+5V0"
- board text added: "+5V0_REG"
- board text added: "+9V0"
- board text added: "ECDR PWR:"
- board text added: "IO PWR STATUS:"
- board text removed: "1Gb NAND FLASH"
- board text removed: "BTN A"
- board text removed: "BTN B"
- board text removed: "CROPTOP v1.0"
- board text removed: "GNSS Reciever"
- board text removed: "IO Terminal Block"
- board text removed: "PIC32MX"
- board text removed: "PICKit3"
- board text removed: "TFT LCD"
- board text removed: "USB 2.0"
- board text removed: "USB 5V"
- board text removed: "ΔΣ ADC"

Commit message: Finished expo prez
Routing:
- net POTEN_ADC_2: track 15.6 -> 40.9 mm
- net POTEN_ADC_1: track 15.7 -> 39.8 mm
- net SONIC_ECHO: track 13.6 -> 35.9 mm
- net ENCDR_A: track 1.42 -> 23.7 mm
- net ~DC_FAULT: track 6.60 -> 28.8 mm
- net DC_PWM_1: track 4.22 -> 26.3 mm
- net SONIC_TRIG: track 12.9 -> 34.9 mm
- net ENCDR_B: track 1.42 -> 22.4 mm
- net DC_PWM_2: track 5.76 -> 26.5 mm

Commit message: Finished PCB
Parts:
- removed FID1, FID2: Fiducial, Fiducial:Fiducial_1mm_Dia_2.54mm_Outer_CopperTop
- removed TP1, TP10, TP11, TP12, TP13, TP14, TP15, TP16, TP17, TP18, TP19, TP2, TP20, TP21, TP22, TP23, TP24, TP25, TP26, TP27, TP28, TP29, TP3, TP30, TP31, TP32, TP33, TP34, TP35, TP36, TP37, TP38, TP39, TP4, TP40, TP41, TP42, TP43, TP44, TP45, TP46, TP47, TP48, TP49, TP5, TP50, TP51, TP52, TP53, TP54, TP55, TP56, TP57, TP58, TP59, TP6, TP60, TP61, TP62, TP63, TP64, TP65, TP66, TP67, TP68, TP69, TP7, TP70, TP71, TP72, TP8, TP9: TestPoint, croptop:TestPoint
- added C4: 12.5p, Capacitor_SMD:C_0402_1005Metric, F.Cu at (144.9, 98.4)
- added C90: 12.5p, Capacitor_SMD:C_0402_1005Metric, F.Cu at (141.7, 98.4)
- added Y3: ABS07-32.768KHZ-1-T, croptop:ABLS_SEC, F.Cu at (143.9, 101.1)
- moved R4 55.8 mm to (100.7, 90.6), turned to 90 degrees
- moved R5 55.8 mm to (103.1, 90.6), turned to 90 degrees
- moved R10 15.9 mm to (130.1, 136.1), turned to 270 degrees
- moved R9 14.9 mm to (130.1, 132.8), turned to 270 degrees
- moved R6 10.6 mm to (147.7, 98.2), turned to 90 degrees
- moved R125 9.65 mm to (89.9, 108.7)
- moved R130 9.65 mm to (89.9, 111.1)
- moved R128 9.65 mm to (88.4, 120.7)
- moved R127 9.53 mm to (89.8, 118.4)
- moved G*** 8.90 mm to (113.8, 97.9)
- moved R7 8.65 mm to (146.2, 98.2), turned to 90 degrees
- moved C8 3.34 mm to (135.8, 100.7), turned to 90 degrees
- moved C12 1.94 mm to (138.8, 100.7)
- moved C15 1.69 mm to (68.5, 127.8), turned to 270 degrees
- moved C13 1.52 mm to (154.3, 110.4)
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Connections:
- U1 pad 1: ~ADI_CS -> Net-(U1-Pad1)
- U1 pad 10: GPU_SCLK -> SD_SCLK
- U1 pad 11: GPU_MISO -> SD_MISO
- U1 pad 12: GPU_MOSI -> SD_MOSI
- U1 pad 33: POTEN_ADC_1 -> POTEN_ADC_2
- U1 pad 34: POTEN_ADC_2 -> POTEN_ADC_1
- U1 pad 4: ~GPU_CS -> Net-(U1-Pad4)
- U1 pad 44: Net-(U1-Pad44) -> Net-(D2-Pad2)
- U1 pad 48: SD_SCLK -> ADI_SCLK
- U1 pad 51: Net-(U1-Pad51) -> ~ADI_CS
- U1 pad 52: SD_MISO -> ADI_MISO
- U1 pad 53: SD_MOSI -> ADI_MOSI
- U1 pad 61: Net-(U1-Pad61) -> ~GPU_CS
- U1 pad 70: ADI_SCLK -> GPU_SCLK
- U1 pad 72: ADI_MOSI -> GPU_MOSI
- U1 pad 74: ~PWR_FAULT -> Net-(C90-Pad1)
- U1 pad 9: ADI_MISO -> GPU_MISO
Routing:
- net ~PWR_FAULT: track 20.4 -> 271.3 mm, vias 0 -> 23
- net DGND: track 465.5 -> 581.8 mm, vias 119 -> 172
- net USB_PWR_EN: track 1.60 -> 107.9 mm, vias 0 -> 4
- net PICKIT_MCLR: track 0.00 -> 99.3 mm, vias 0 -> 6
- net USB_PWR_SENSE: track 13.0 -> 105.1 mm
- net PICKIT_PGEC: track 0.00 -> 87.5 mm, vias 0 -> 6
- net PMOD_SCL: track 4.39 -> 89.3 mm, vias 1 -> 5
- net PMOD_TX: track 2.51 -> 86.4 mm, vias 1 -> 6
- net PICKIT_PGED: track 0.00 -> 83.4 mm, vias 0 -> 6
- net PMOD_RX: track 5.76 -> 87.9 mm, vias 1 -> 6
- net PMOD_SDA: track 4.68 -> 86.2 mm, vias 2 -> 6
- net ~STEP_HOME: track 0.00 -> 80.1 mm, vias 0 -> 2
- net PMOD_ADC_4: track 4.24 -> 82.6 mm, vias 1 -> 6
- net GPU_PWM: track 9.11 -> 85.5 mm, vias 1 -> 5
- net PMOD_ADC_3: track 4.56 -> 79.1 mm, vias 2 -> 7
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- added copper zone on B.Cu, net DGND

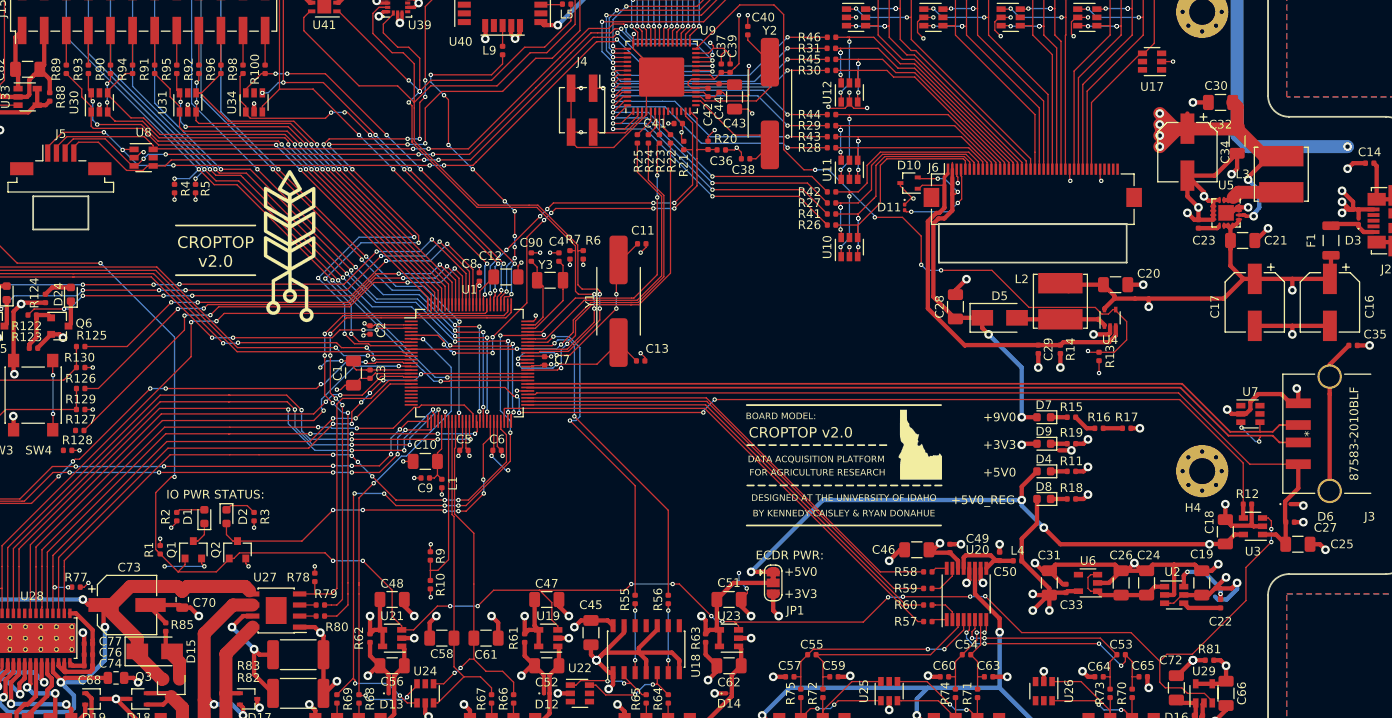
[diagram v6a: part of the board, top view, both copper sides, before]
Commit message: Updated PCB2, Changed MotorLib, Changed PotLib
- Updated PCB2 to have all correct MPNs
- Added some useful macros within the standard hardware heade file
- Changed hardware initialization function calls (for main, MotorLib, and PotLib) to return an error flag.
- Corrected GPIO configurations for switches, LEDS
- Made initialize_system() private
- Added Doxygen to MotorLib and PotLib files
- Reduced bloat of MotorLib by combining subsystem setup functions into one.
- Added boundary condition checks for PWM functions
- Added error-flag return values to motor functions
- Corrected issue where CN14 was "used" to detect faults, but in PCBv2.2 CN14 is connected to GPU_INT, and INT1 is connected to DC_FAULT. Updated code accordingly.
- Made ADC / Potentiometer functionality "smart" configure T3 to sample the ADC at a variable, desired frequency.
- Updated potentiometer configuration to use AN9 and AN10
- Added error-flag returns to initialize_potentiometer()
- Added ISR for timer 3 that is used to trigger ADC samples automatically
- Added multi-inclusion protection to all currently-addressed files (will do rest later)

** THIS HAS NOT BEEN COMPILE VERIFIED - CHECK WITH XC32 COMPILER **
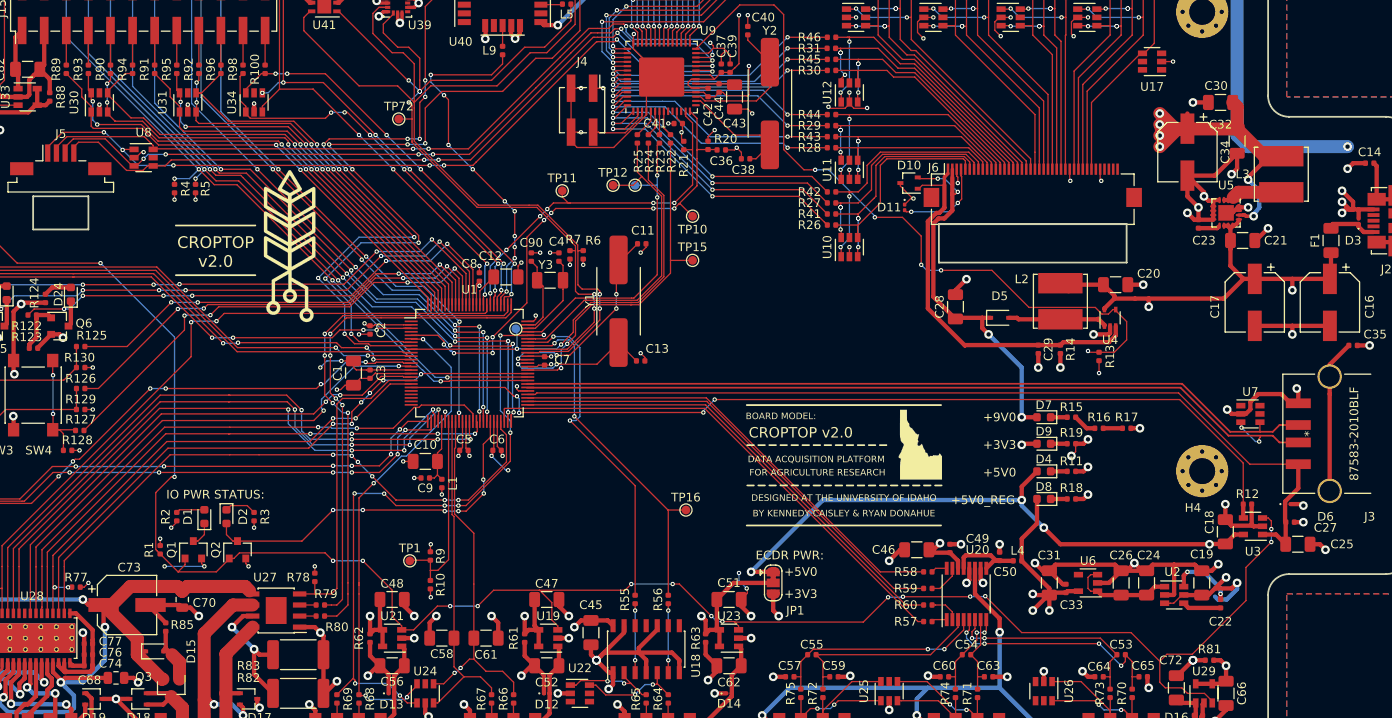
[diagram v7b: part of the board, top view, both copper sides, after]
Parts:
- added TP1: TestPoint, TestPoint:TestPoint_Pad_D1.0mm, F.Cu at (127.8, 133.3)
- added TP10: TestPoint, TestPoint:TestPoint_Pad_D1.0mm, F.Cu at (160.3, 93.7)
- added TP11: TestPoint, TestPoint:TestPoint_Pad_D1.0mm, F.Cu at (145.3, 90.8)
- added TP12: TestPoint, TestPoint:TestPoint_Pad_D1.0mm, F.Cu at (151.1, 90.2)
- added TP13: TestPoint, TestPoint:TestPoint_Pad_D1.0mm, F.Cu at (140.0, 106.7)
- added TP14: TestPoint, TestPoint:TestPoint_Pad_D1.0mm, F.Cu at (153.7, 90.2)
- added TP15: TestPoint, TestPoint:TestPoint_Pad_D1.0mm, F.Cu at (160.3, 98.8)
- added TP16: TestPoint, TestPoint:TestPoint_Pad_D1.0mm, F.Cu at (159.5, 127.5)
- added TP72: TestPoint, TestPoint:TestPoint_Pad_D1.0mm, F.Cu at (126.5, 82.5)
- D15, D5: footprint Diode_SMD:D_SMA -> Diode_SMD:D_SOD-323
- F1: footprint croptop:Bourns_Fuse -> Fuse:Fuse_1206_3216Metric
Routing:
- net Net-(R127-Pad2): track 8.24 -> 14.2 mm
- net GPU_SCLK: track 34.8 -> 38.5 mm
- net GPU_MOSI: track 32.8 -> 35.4 mm
- net ~GPU_CS: track 38.3 -> 40.8 mm
- net CONFIG_ADC: track 20.9 -> 23.3 mm
- net GPU_MISO: track 49.6 -> 51.9 mm
- net ~GPU_PWR_DWN: track 58.6 -> 60.8 mm
- net ENCDR_A: track 39.1 -> 41.2 mm
- net ~GPU_INT: track 41.4 -> 43.2 mm
- net ONBRD_SDA: track 98.5 -> 100.1 mm
- net Net-(C68-Pad1): track 93.4 -> 94.6 mm
- net DGND: track 581.8 -> 582.9 mm
- net Net-(D5-Pad2): track 10.6 -> 11.5 mm
